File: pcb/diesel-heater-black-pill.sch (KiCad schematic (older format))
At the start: 26 parts, among them J1 5V Power, J10 Motor, J11 Glow Plug, J12 Oil Plug, J2 Black Pill Left, J3 Black Pill Right, J4 Buttons, J5 Hall Sensor, J6 Battery Mon, J7 OLED, J8 NTC50K Room Temperature, J9 NTC50K Outlet Temperature

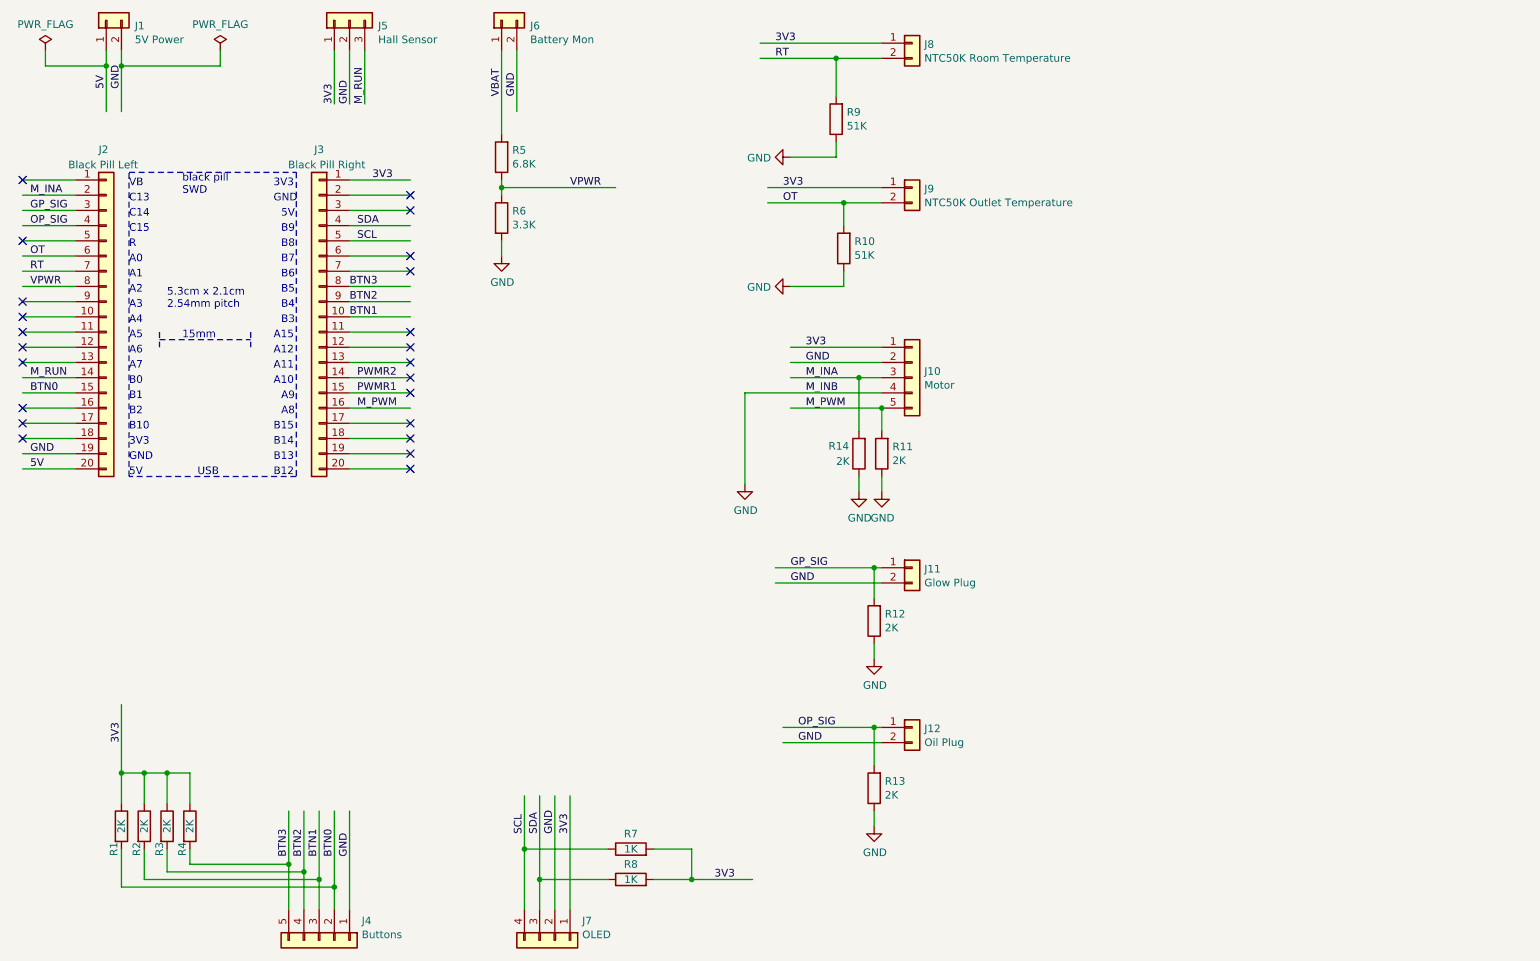
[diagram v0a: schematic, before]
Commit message: changed pcb to add esp-01
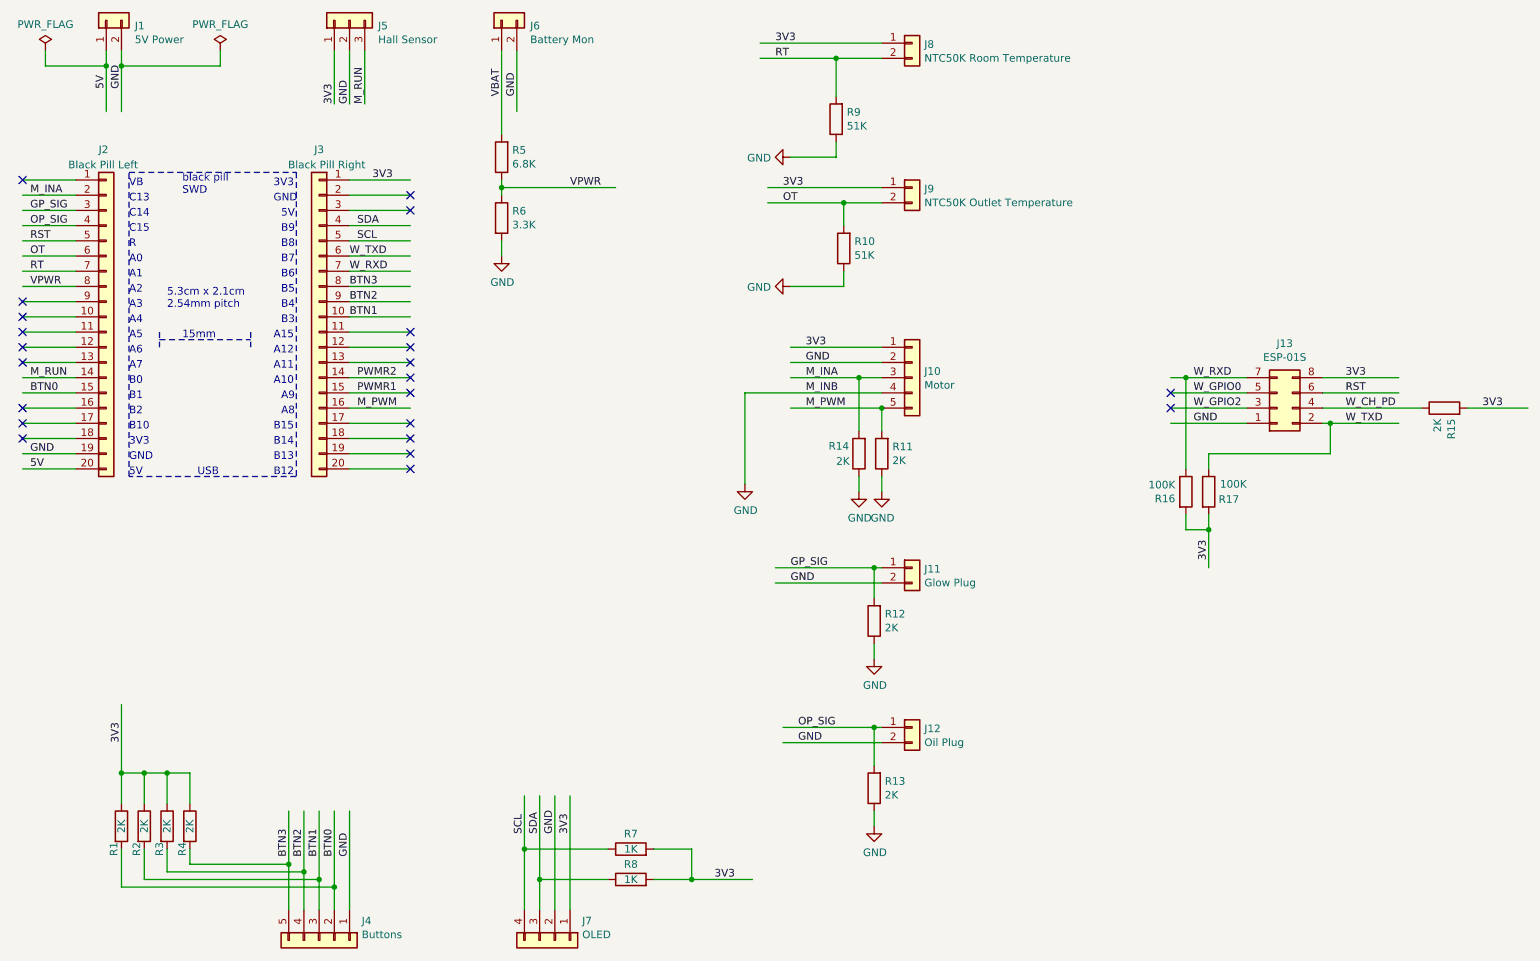
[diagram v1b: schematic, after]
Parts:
- added J13: ESP-01S, Connector_PinSocket_2.54mm:PinSocket_2x04_P2.54mm_Vertical, symbol Connector_Generic:Conn_02x04_Odd_Even
- added R15: 2K, Resistor_SMD:R_0603_1608Metric_Pad0.98x0.95mm_HandSolder, symbol Device:R
- added R16, R17: 100K, Resistor_SMD:R_0603_1608Metric_Pad0.98x0.95mm_HandSolder, symbol Device:R
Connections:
- net labels added: RST, W_CH_PD, W_GPIO0, W_GPIO2, W_RXD, W_TXD
- wire segments 127 -> 146
- no-connect marks 23 -> 22
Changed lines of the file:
@@
 NoConn ~ 800  2700
 NoConn ~ 800  2600
-NoConn ~ 800  2200
 NoConn ~ 3350 3700
 NoConn ~ 3350 3600
@@
 NoConn ~ 3350 2900
 NoConn ~ 3350 2800
-NoConn ~ 3350 2400
-NoConn ~ 3350 2300
 Text Label 3000 3200 0    50   ~ 0
 PWMR1
@@
 Wire Wire Line
 	4200 6400 4200 5850
+$Comp
+L Connector_Generic:Conn_02x04_Odd_Even J13
+U 1 1 60388E75
+P 9050 3300
+F 0 "J13" H 9100 2875 50  0000 C CNN
+F 1 "ESP-01S" H 9100 2966 50  0000 C CNN
+F 2 "Connector_PinSocket_2.54mm:PinSocket_2x04_P2.54mm_Vertical" H 9050 3300 50  0001 C CNN
+F 3 "~" H 9050 3300 50  0001 C CNN
+	1    9050 3300
+	1    0    0    1
+$EndComp
+Wire Wire Line
+	8850 3400 8350 3400
+Wire Wire Line
+	9350 3100 9850 3100
+Wire Wire Line
+	8850 3300 8350 3300
+Wire Wire Line
+	8850 3200 8350 3200
+Text Label 8500 3400 0    50   ~ 0
+GND
+Text Label 9500 3400 0    50   ~ 0
+W_TXD
+Text Label 8500 3300 0    50   ~ 0
+W_GPIO2
+Text Label 9500 3300 0    50   ~ 0
+W_CH_PD
+Text Label 8500 3200 0    50   ~ 0
+W_GPIO0
+Text Label 8500 3100 0    50   ~ 0
+W_RXD
+Text Label 9500 3100 0    50   ~ 0
+3V3
+NoConn ~ 8350 3300
+NoConn ~ 8350 3200
+Wire Wire Line
+	9350 3200 9850 3200
+Text Label 9500 3200 0    50   ~ 0
+RST
+$Comp
+L Device:R R15
+U 1 1 603EBB53
+P 10150 3300
+F 0 "R15" H 10080 3254 50  0000 R CNN
+F 1 "2K" H 10080 3345 50  0000 R CNN
+F 2 "Resistor_SMD:R_0603_1608Metric_Pad0.98x0.95mm_HandSolder" V 10080 3300 50  0001 C CNN
+F 3 "~" H 10150 3300 50  0001 C CNN
+	1    10150 3300
+	0    -1   -1   0
+$EndComp
+Text Label 850  2200 0    50   ~ 0
+RST
+Text Label 2950 2400 0    50   ~ 0
+W_RXD
+Text Label 2950 2300 0    50   ~ 0
+W_TXD
+Wire Wire Line
+	9350 3300 10000 3300
+Wire Wire Line
+	10300 3300 10700 3300
+Text Label 10400 3300 0    50   ~ 0
+3V3
+$Comp
+L Device:R R16
+U 1 1 60413BA0
+P 8450 3850
+F 0 "R16" H 8380 3804 50  0000 R CNN
+F 1 "100K" H 8380 3895 50  0000 R CNN
+F 2 "Resistor_SMD:R_0603_1608Metric_Pad0.98x0.95mm_HandSolder" V 8380 3850 50  0001 C CNN
+F 3 "~" H 8450 3850 50  0001 C CNN
+	1    8450 3850
+	1    0    0    -1
+$EndComp
+Wire Wire Line
+	8350 3100 8450 3100
+Wire Wire Line
+	8450 3700 8450 3100
+Connection ~ 8450 3100
+Wire Wire Line
+	8450 3100 8850 3100
+$Comp
+L Device:R R17
+U 1 1 60418DD4
+P 8600 3850
+F 0 "R17" H 8800 3800 50  0000 R CNN
+F 1 "100K" H 8850 3900 50  0000 R CNN
+F 2 "Resistor_SMD:R_0603_1608Metric_Pad0.98x0.95mm_HandSolder" V 8530 3850 50  0001 C CNN
+F 3 "~" H 8600 3850 50  0001 C CNN
+	1    8600 3850
+	1    0    0    -1
+$EndComp
+Wire Wire Line
+	9400 3400 9400 3600
+Wire Wire Line
+	9400 3600 8600 3600
+Wire Wire Line
+	8600 3600 8600 3700
+Wire Wire Line
+	9350 3400 9400 3400
+Connection ~ 9400 3400
+Wire Wire Line
+	9400 3400 9850 3400
+Wire Wire Line
+	8450 4000 8450 4100
+Wire Wire Line
+	8450 4100 8600 4100
+Wire Wire Line
+	8600 4000 8600 4100
+Wire Wire Line
+	8600 4100 8600 4350
+Connection ~ 8600 4100
+Text Label 8600 4300 1    50   ~ 0
+3V3
 $EndSCHEMATC

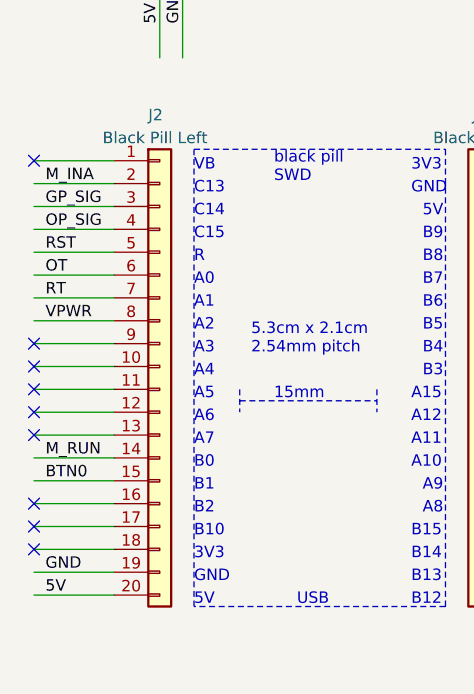
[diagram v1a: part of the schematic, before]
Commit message: changed to use PB10 for motor INA
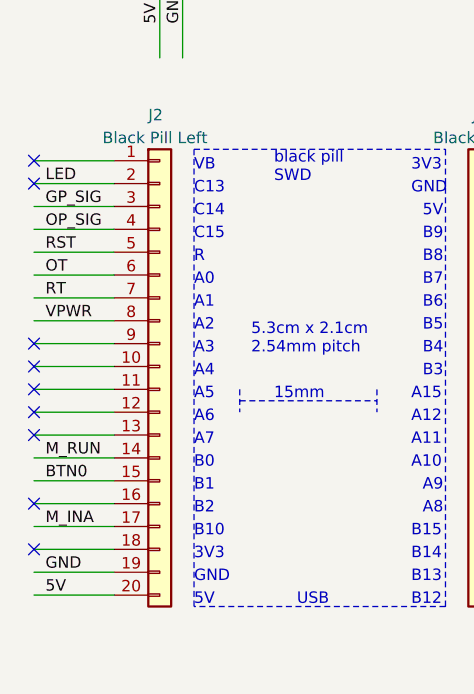
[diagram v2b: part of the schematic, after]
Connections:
- net labels added: LED
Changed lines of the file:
@@
 Text Label 2950 2500 0    50   ~ 0
 BTN3
-NoConn ~ 800  3400
 NoConn ~ 800  3300
 NoConn ~ 800  3000
@@
 PWMR2
 Text Label 850  1900 0    50   ~ 0
-M_INA
+LED
 Wire Wire Line
 	6450 3100 6300 3100
@@
 Text Label 8600 4300 1    50   ~ 0
 3V3
+NoConn ~ 800  1900
+Text Label 850  3400 0    50   ~ 0
+M_INA
 $EndSCHEMATC

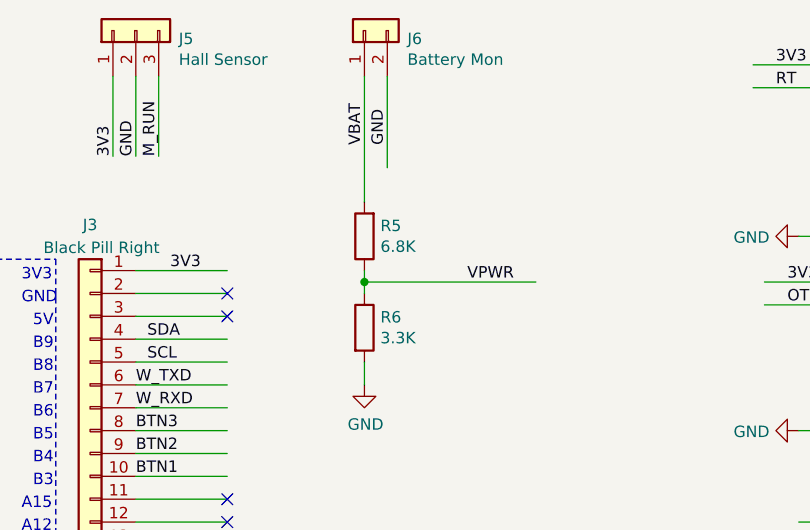
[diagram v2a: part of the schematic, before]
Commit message: changed main power batter voltage divider from 6.3K to 33K
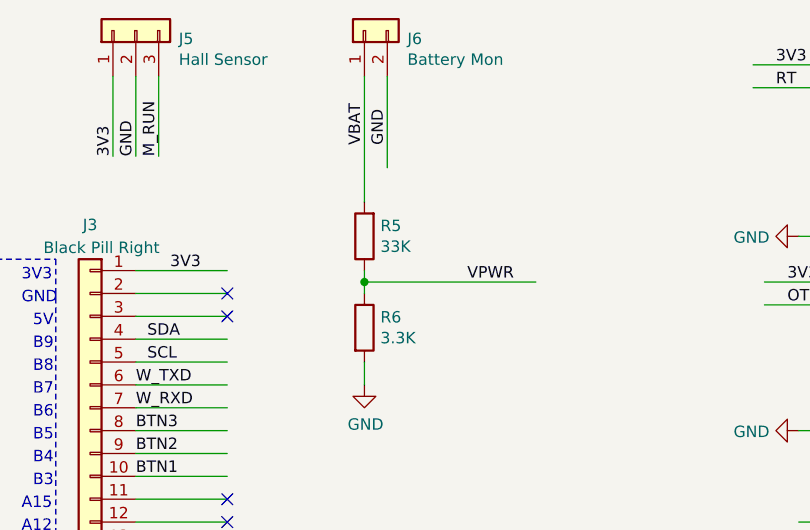
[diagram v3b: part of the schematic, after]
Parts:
- R5: value 6.8K -> 33K
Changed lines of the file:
@@
 P 3950 1650
 F 0 "R5" H 3880 1604 50  0000 R CNN
-F 1 "6.8K" H 3880 1695 50  0000 R CNN
+F 1 "33K" H 3880 1695 50  0000 R CNN
 F 2 "Resistor_SMD:R_0603_1608Metric_Pad0.98x0.95mm_HandSolder" V 3880 1650 50  0001 C CNN
 F 3 "~" H 3950 1650 50  0001 C CNN
